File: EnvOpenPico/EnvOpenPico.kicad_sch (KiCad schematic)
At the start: 61 parts, among them J2 SKRKAEE020, J3 2.54mm header 01x20, J4 2.54mm header 01x20, J5 Conn_01x03_Male, Q1 Si2329DS, U1 TLV75533PDBVR, U2 24LC256, U3 RP2040, Y1 3225_4P

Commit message: updated readme
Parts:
- FLASH1: value ZD25WQ16BUIGR -> w25q16jvuxiq
- R12, R8: value 10K 0402 Resistor -> 10K 0402
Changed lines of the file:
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@@
     (in_bom yes) (on_board yes)
     (property "Reference" "FLASH1" (id 0) (at 78.74 133.35 0))
-    (property "Value" "ZD25WQ16BUIGR" (id 1) (at 78.74 146.05 0))
+    (property "Value" "w25q16jvuxiq" (id 1) (at 78.74 146.05 0))
     (property "Footprint" "Package_SON:SON-8-1EP_3x2mm_P0.5mm_EP1.4x1.6mm" (id 2) (at 78.74 133.35 0)
       (effects (font (size 1.27 1.27)) (justify left bottom) hide)
@@
     (in_bom yes) (on_board yes)
     (property "Reference" "R12" (id 0) (at 71.12 203.2 90))
-    (property "Value" "10K 0402 Resistor" (id 1) (at 68.1736 203.2 90)
+    (property "Value" "10K 0402" (id 1) (at 68.1736 203.2 90)
       (effects (font (size 1.27 1.27)) hide)
     )
@@
     (in_bom yes) (on_board yes)
     (property "Reference" "R8" (id 0) (at 67.31 200.66 90))
-    (property "Value" "10K 0402 Resistor" (id 1) (at 64.3636 200.66 90)
+    (property "Value" "10K 0402" (id 1) (at 64.3636 200.66 90)
       (effects (font (size 1.27 1.27)) hide)
     )
@@
     )
     (path "/00000000-0000-0000-0000-0000608edada"
-      (reference "FLASH1") (unit 1) (value "ZD25WQ16BUIGR") (footprint "Package_SON:SON-8-1EP_3x2mm_P0.5mm_EP1.4x1.6mm")
+      (reference "FLASH1") (unit 1) (value "w25q16jvuxiq") (footprint "Package_SON:SON-8-1EP_3x2mm_P0.5mm_EP1.4x1.6mm")
     )
     (path "/00000000-0000-0000-0000-000061cdafdc"
@@
     )
     (path "/a68b9feb-2131-49da-8507-cc49a7fd0362"
-      (reference "R8") (unit 1) (value "10K 0402 Resistor") (footprint "Resistor_SMD:R_0402_1005Metric")
+      (reference "R8") (unit 1) (value "10K 0402") (footprint "Resistor_SMD:R_0402_1005Metric")
     )
     (path "/00000000-0000-0000-0000-000061044b24"
@@
     )
     (path "/744288eb-ceb8-4c6c-94d9-d7176b3f8b7b"
-      (reference "R12") (unit 1) (value "10K 0402 Resistor") (footprint "Resistor_SMD:R_0402_1005Metric")
+      (reference "R12") (unit 1) (value "10K 0402") (footprint "Resistor_SMD:R_0402_1005Metric")
     )
     (path "/f3e05f83-9b50-4acb-a83a-0b490aa727ec"

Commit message: faff and things, no important changes.
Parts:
- FLASH1: value w25q16jvuxiq -> W25Q16JV
- U1: value TLV75533PDBVR -> TLV75733PDBVR
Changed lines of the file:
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@@
     (in_bom yes) (on_board yes)
     (property "Reference" "FLASH1" (id 0) (at 78.74 133.35 0))
-    (property "Value" "w25q16jvuxiq" (id 1) (at 78.74 146.05 0))
+    (property "Value" "W25Q16JV" (id 1) (at 78.74 146.05 0))
     (property "Footprint" "Package_SON:SON-8-1EP_3x2mm_P0.5mm_EP1.4x1.6mm" (id 2) (at 78.74 133.35 0)
       (effects (font (size 1.27 1.27)) (justify left bottom) hide)
@@
     (in_bom yes) (on_board yes)
     (property "Reference" "U1" (id 0) (at 110.49 38.3032 0))
-    (property "Value" "TLV75533PDBVR" (id 1) (at 110.49 40.6146 0))
+    (property "Value" "TLV75733PDBVR" (id 1) (at 110.49 40.6146 0))
     (property "Footprint" "Package_TO_SOT_SMD:SOT-23-5" (id 2) (at 110.49 38.735 0)
       (effects (font (size 1.27 1.27) italic) hide)
@@
     )
     (path "/00000000-0000-0000-0000-0000608edada"
-      (reference "FLASH1") (unit 1) (value "w25q16jvuxiq") (footprint "Package_SON:SON-8-1EP_3x2mm_P0.5mm_EP1.4x1.6mm")
+      (reference "FLASH1") (unit 1) (value "W25Q16JV") (footprint "Package_SON:SON-8-1EP_3x2mm_P0.5mm_EP1.4x1.6mm")
     )
     (path "/00000000-0000-0000-0000-000061cdafdc"
@@
     )
     (path "/00000000-0000-0000-0000-00006128f962"
-      (reference "U1") (unit 1) (value "TLV75533PDBVR") (footprint "Package_TO_SOT_SMD:SOT-23-5")
+      (reference "U1") (unit 1) (value "TLV75733PDBVR") (footprint "Package_TO_SOT_SMD:SOT-23-5")
     )
     (path "/a29ee7c4-9a3e-4dd1-8608-a5d1bfaa06bd"

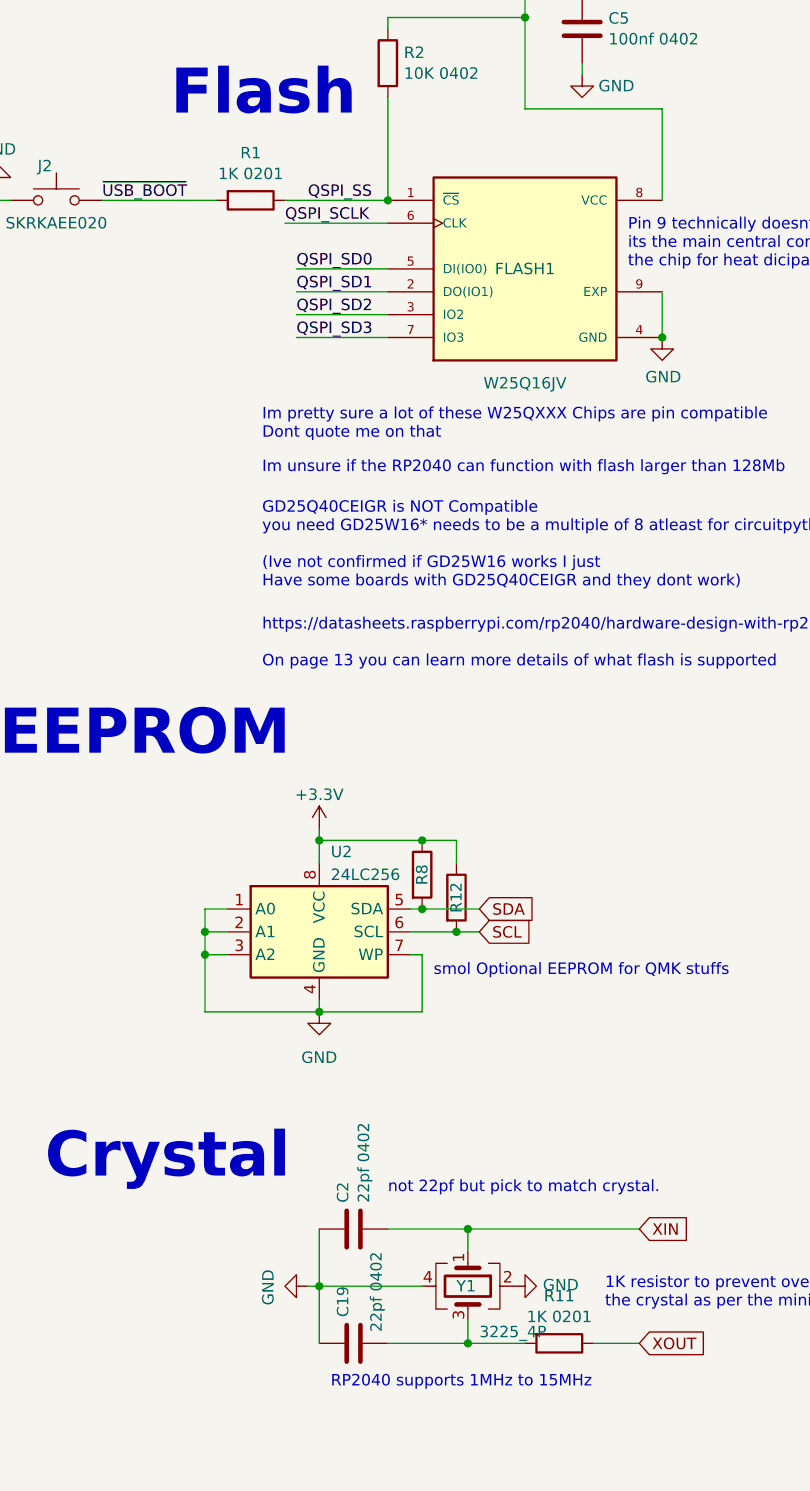
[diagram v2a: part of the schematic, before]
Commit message: lots of changes, swapped many parts to 0402, swapped SOT regulator to small WSON, made sure there is proper parity between footprint and value, etc etc etc
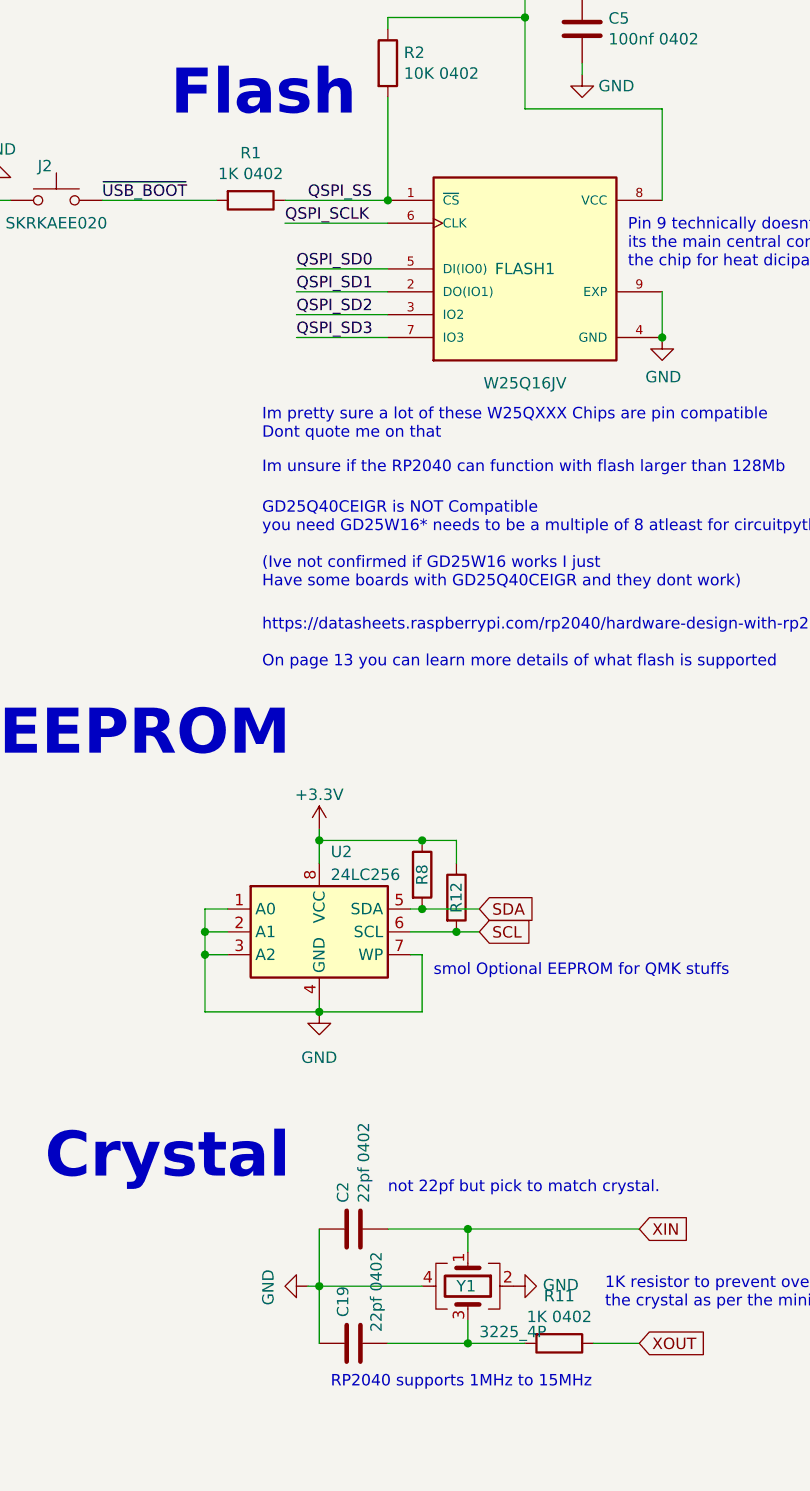
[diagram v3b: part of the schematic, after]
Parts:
- R1, R11: value 1K 0201 -> 1K 0402; footprint Resistor_SMD:R_0201_0603Metric -> Resistor_SMD:R_0402_1005Metric
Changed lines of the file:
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@@
     (in_bom yes) (on_board yes)
     (property "Reference" "R1" (id 0) (at 48.26 120.4722 90))
-    (property "Value" "1K 0201" (id 1) (at 48.26 122.7836 90))
-    (property "Footprint" "Resistor_SMD:R_0201_0603Metric" (id 2) (at 48.26 123.952 90)
+    (property "Value" "1K 0402" (id 1) (at 48.26 122.7836 90))
+    (property "Footprint" "Resistor_SMD:R_0402_1005Metric" (id 2) (at 48.26 123.952 90)
       (effects (font (size 1.27 1.27)) hide)
     )
@@
     (in_bom yes) (on_board yes)
     (property "Reference" "R11" (id 0) (at 82.55 247.4722 90))
-    (property "Value" "1K 0201" (id 1) (at 82.55 249.7836 90))
-    (property "Footprint" "Resistor_SMD:R_0201_0603Metric" (id 2) (at 82.55 250.952 90)
+    (property "Value" "1K 0402" (id 1) (at 82.55 249.7836 90))
+    (property "Footprint" "Resistor_SMD:R_0402_1005Metric" (id 2) (at 82.55 250.952 90)
       (effects (font (size 1.27 1.27)) hide)
     )
@@
     )
     (path "/00000000-0000-0000-0000-00005edae9f0"
-      (reference "R1") (unit 1) (value "1K 0201") (footprint "Resistor_SMD:R_0201_0603Metric")
+      (reference "R1") (unit 1) (value "1K 0402") (footprint "Resistor_SMD:R_0402_1005Metric")
     )
     (path "/00000000-0000-0000-0000-00005edac067"
@@
     )
     (path "/00000000-0000-0000-0000-00006150e6ab"
-      (reference "R11") (unit 1) (value "1K 0201") (footprint "Resistor_SMD:R_0201_0603Metric")
+      (reference "R11") (unit 1) (value "1K 0402") (footprint "Resistor_SMD:R_0402_1005Metric")
     )
     (path "/744288eb-ceb8-4c6c-94d9-d7176b3f8b7b"

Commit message: made some smaller components generated new gerber
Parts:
- J2, RSW1: value SKRKAEE020 -> TSA343G00-250J2
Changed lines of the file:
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@@
     (in_bom yes) (on_board yes)
     (property "Reference" "J2" (id 0) (at 25.4 121.92 0))
-    (property "Value" "SKRKAEE020" (id 1) (at 26.67 128.27 0))
+    (property "Value" "TSA343G00-250J2" (id 1) (at 26.67 128.27 0))
     (property "Footprint" "Button_Switch_SMD:SW_Push_SPST_NO_Alps_SKRK" (id 2) (at 26.67 125.73 0)
       (effects (font (size 1.27 1.27)) hide)
@@
     (in_bom yes) (on_board yes)
     (property "Reference" "RSW1" (id 0) (at 144.78 170.18 0))
-    (property "Value" "SKRKAEE020" (id 1) (at 146.05 167.64 0))
+    (property "Value" "TSA343G00-250J2" (id 1) (at 146.05 167.64 0))
     (property "Footprint" "Button_Switch_SMD:SW_Push_SPST_NO_Alps_SKRK" (id 2) (at 144.78 165.1 0)
       (effects (font (size 1.27 1.27)) hide)
@@
     )
     (path "/00000000-0000-0000-0000-00005f30f0ba"
-      (reference "J2") (unit 1) (value "SKRKAEE020") (footprint "Button_Switch_SMD:SW_Push_SPST_NO_Alps_SKRK")
+      (reference "J2") (unit 1) (value "TSA343G00-250J2") (footprint "Button_Switch_SMD:SW_Push_SPST_NO_Alps_SKRK")
     )
     (path "/00000000-0000-0000-0000-00005f4b4ce4"
@@
     )
     (path "/00000000-0000-0000-0000-00006142c001"
-      (reference "RSW1") (unit 1) (value "SKRKAEE020") (footprint "Button_Switch_SMD:SW_Push_SPST_NO_Alps_SKRK")
+      (reference "RSW1") (unit 1) (value "TSA343G00-250J2") (footprint "Button_Switch_SMD:SW_Push_SPST_NO_Alps_SKRK")
     )
     (path "/00000000-0000-0000-0000-00006102353c"

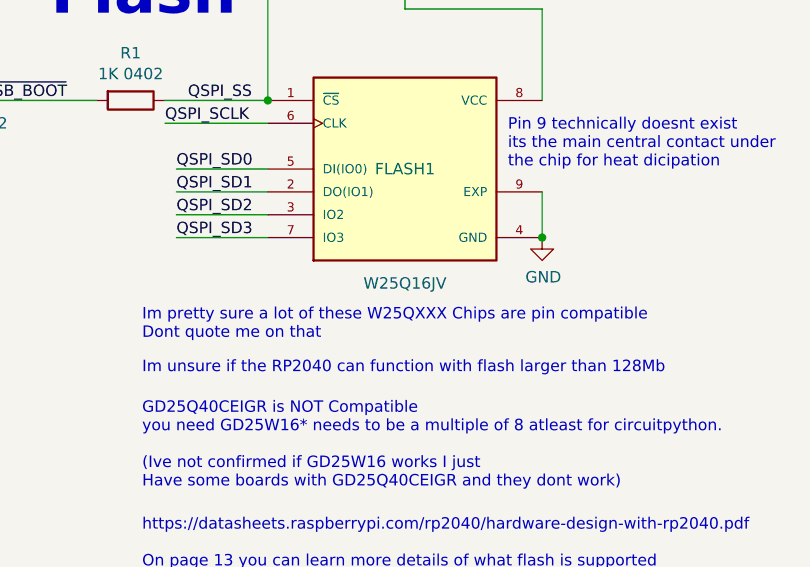
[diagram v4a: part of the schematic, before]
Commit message: swapped flash for one that was in stock.
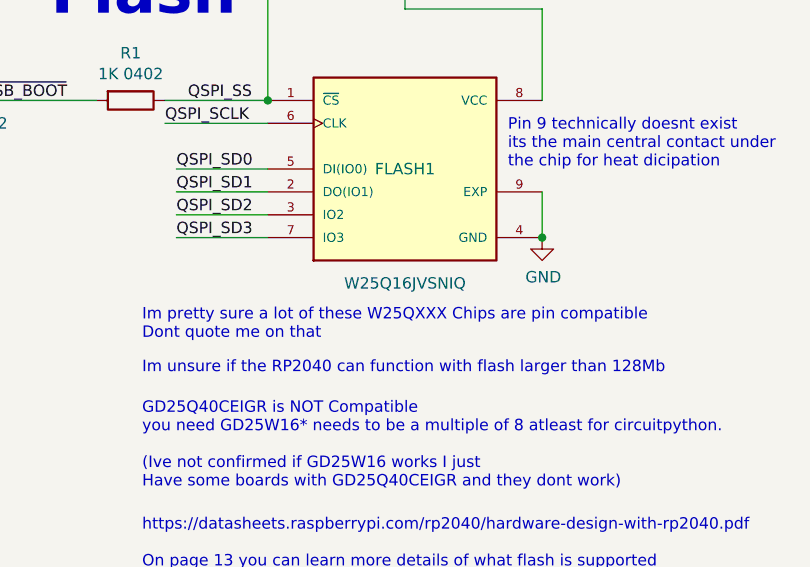
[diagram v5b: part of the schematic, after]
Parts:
- FLASH1: value W25Q16JV -> W25Q16JVSNIQ; footprint Package_SON:SON-8-1EP_3x2mm_P0.5mm_EP1.4x1.6mm -> Package_SO:SO-8_3.9x4.9mm_P1.27mm
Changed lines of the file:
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@@
     (in_bom yes) (on_board yes)
     (property "Reference" "FLASH1" (id 0) (at 78.74 133.35 0))
-    (property "Value" "W25Q16JV" (id 1) (at 78.74 146.05 0))
-    (property "Footprint" "Package_SON:SON-8-1EP_3x2mm_P0.5mm_EP1.4x1.6mm" (id 2) (at 78.74 133.35 0)
+    (property "Value" "W25Q16JVSNIQ" (id 1) (at 78.74 146.05 0))
+    (property "Footprint" "Package_SO:SO-8_3.9x4.9mm_P1.27mm" (id 2) (at 78.74 133.35 0)
       (effects (font (size 1.27 1.27)) (justify left bottom) hide)
     )
@@
     )
     (path "/00000000-0000-0000-0000-0000608edada"
-      (reference "FLASH1") (unit 1) (value "W25Q16JV") (footprint "Package_SON:SON-8-1EP_3x2mm_P0.5mm_EP1.4x1.6mm")
+      (reference "FLASH1") (unit 1) (value "W25Q16JVSNIQ") (footprint "Package_SO:SO-8_3.9x4.9mm_P1.27mm")
     )
     (path "/00000000-0000-0000-0000-000061cdafdc"

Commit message: various updates including README
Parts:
- R3, R4: value 27 0402 -> 27r 0402 resistor
- U1: value TLV75733PDBVR -> SOT-23-5 5.5V 3.3V 500mA
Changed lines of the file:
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@@
     (in_bom yes) (on_board yes)
     (property "Reference" "R3" (id 0) (at 245.11 91.2622 90))
-    (property "Value" "27 0402" (id 1) (at 245.11 93.5736 90))
+    (property "Value" "27r 0402 resistor" (id 1) (at 245.11 93.5736 90))
     (property "Footprint" "Resistor_SMD:R_0402_1005Metric" (id 2) (at 245.11 94.742 90)
       (effects (font (size 1.27 1.27)) hide)
@@
     (in_bom yes) (on_board yes)
     (property "Reference" "R4" (id 0) (at 245.11 98.8822 90))
-    (property "Value" "27 0402" (id 1) (at 245.11 101.1936 90))
+    (property "Value" "27r 0402 resistor" (id 1) (at 245.11 101.1936 90))
     (property "Footprint" "Resistor_SMD:R_0402_1005Metric" (id 2) (at 245.11 102.362 90)
       (effects (font (size 1.27 1.27)) hide)
@@
     (in_bom yes) (on_board yes)
     (property "Reference" "U1" (id 0) (at 110.49 38.3032 0))
-    (property "Value" "TLV75733PDBVR" (id 1) (at 110.49 40.6146 0))
+    (property "Value" "SOT-23-5 5.5V 3.3V 500mA" (id 1) (at 110.49 40.6146 0))
     (property "Footprint" "Package_TO_SOT_SMD:SOT-23-5" (id 2) (at 110.49 38.735 0)
       (effects (font (size 1.27 1.27) italic) hide)
@@
     )
     (path "/00000000-0000-0000-0000-00005ede0881"
-      (reference "R3") (unit 1) (value "27 0402") (footprint "Resistor_SMD:R_0402_1005Metric")
+      (reference "R3") (unit 1) (value "27r 0402 resistor") (footprint "Resistor_SMD:R_0402_1005Metric")
     )
     (path "/00000000-0000-0000-0000-00005ede1624"
-      (reference "R4") (unit 1) (value "27 0402") (footprint "Resistor_SMD:R_0402_1005Metric")
+      (reference "R4") (unit 1) (value "27r 0402 resistor") (footprint "Resistor_SMD:R_0402_1005Metric")
     )
     (path "/00000000-0000-0000-0000-00006093a5b0"
@@
     )
     (path "/00000000-0000-0000-0000-00006128f962"
-      (reference "U1") (unit 1) (value "TLV75733PDBVR") (footprint "Package_TO_SOT_SMD:SOT-23-5")
+      (reference "U1") (unit 1) (value "SOT-23-5 5.5V 3.3V 500mA") (footprint "Package_TO_SOT_SMD:SOT-23-5")
     )
     (path "/a29ee7c4-9a3e-4dd1-8608-a5d1bfaa06bd"

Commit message: incr version, added mosfet and led for GP23, marked GP24, tiny bits of cleanup and DRC checks.
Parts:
- removed R12, R8: 10K 0402, Resistor_SMD:R_0402_1005Metric, symbol Device:R
- removed U2: 24LC256, Package_DFN_QFN:TDFN-8-1EP_3x2mm_P0.5mm_EP1.3x1.4mm, symbol Memory_EEPROM:24LC256
- FLASH1: value W25Q16JVSNIQ -> W25Q16JVUXIQ; footprint Package_SO:SO-8_3.9x4.9mm_P1.27mm -> Package_SON:SON-8-1EP_3x2mm_P0.5mm_EP1.4x1.6mm
- GP23_LED1: renamed from GPIO24_LED1; value LED_0402 -> GP23 LED_0402
- GPIO24_RESISTOR1: value 470 0402 -> 1K 0402
- Q1: value Si2329DS -> SI2301B
- R102: value 1M 0402 -> 220 0402
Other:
- note removed: "EEPROM"
- note removed: "smol Optional EEPROM for QMK stuffs"
